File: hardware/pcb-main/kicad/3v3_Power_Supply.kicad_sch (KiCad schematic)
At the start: 15 parts, among them U1 MP2393GTL-P

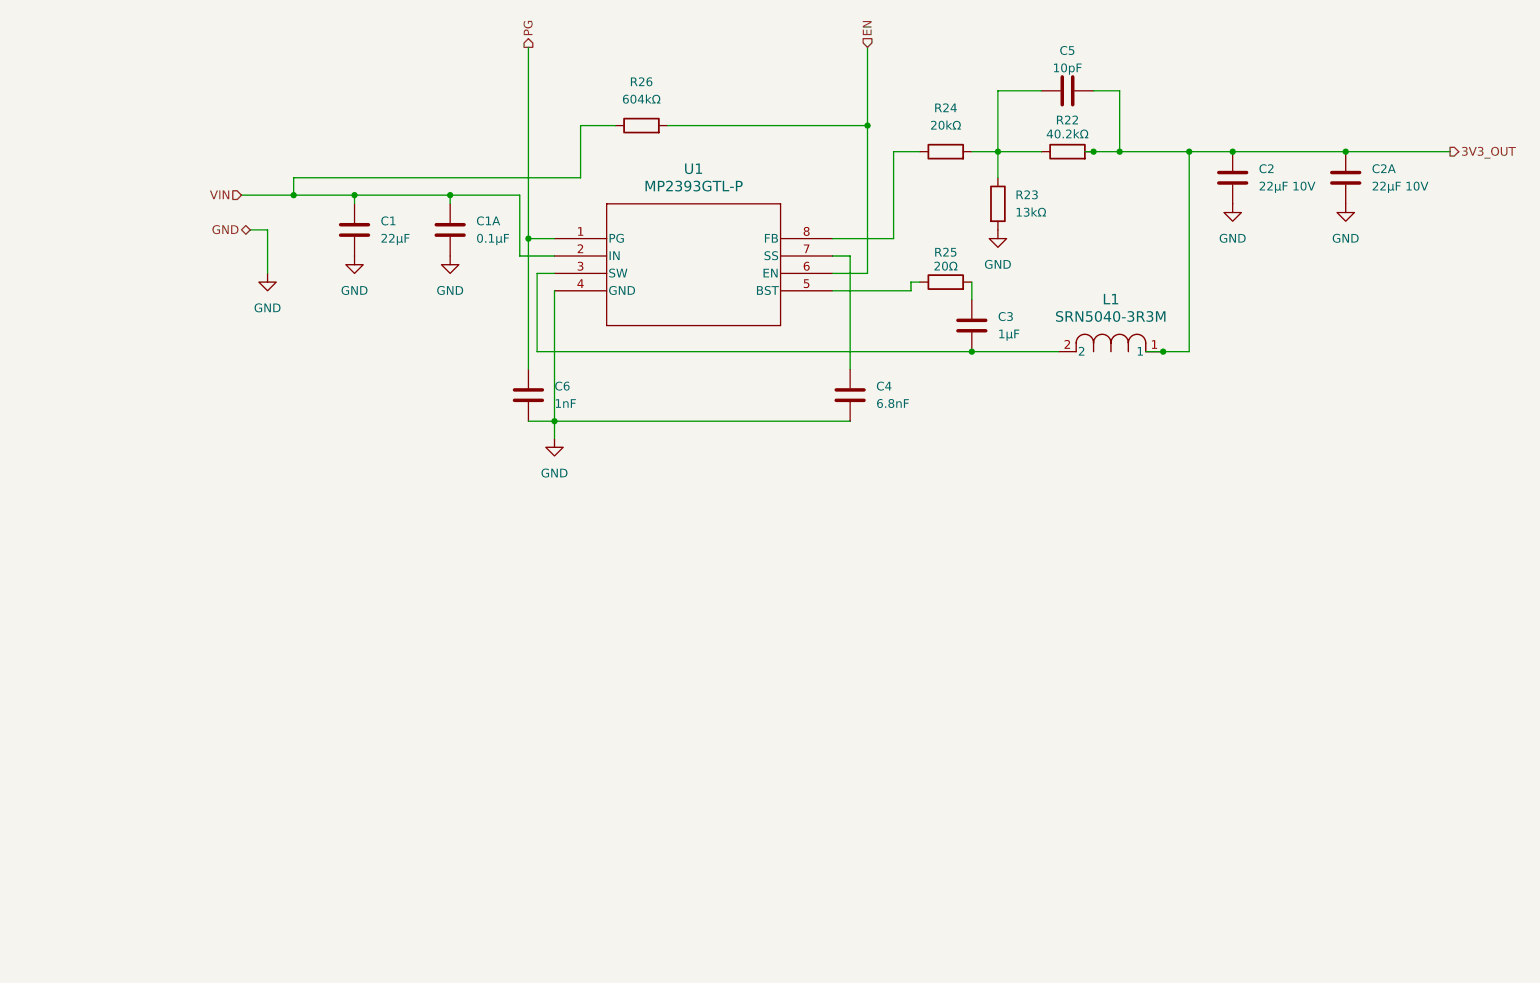
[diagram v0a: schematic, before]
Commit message: Updated to use ultra simplified 3v buck converter
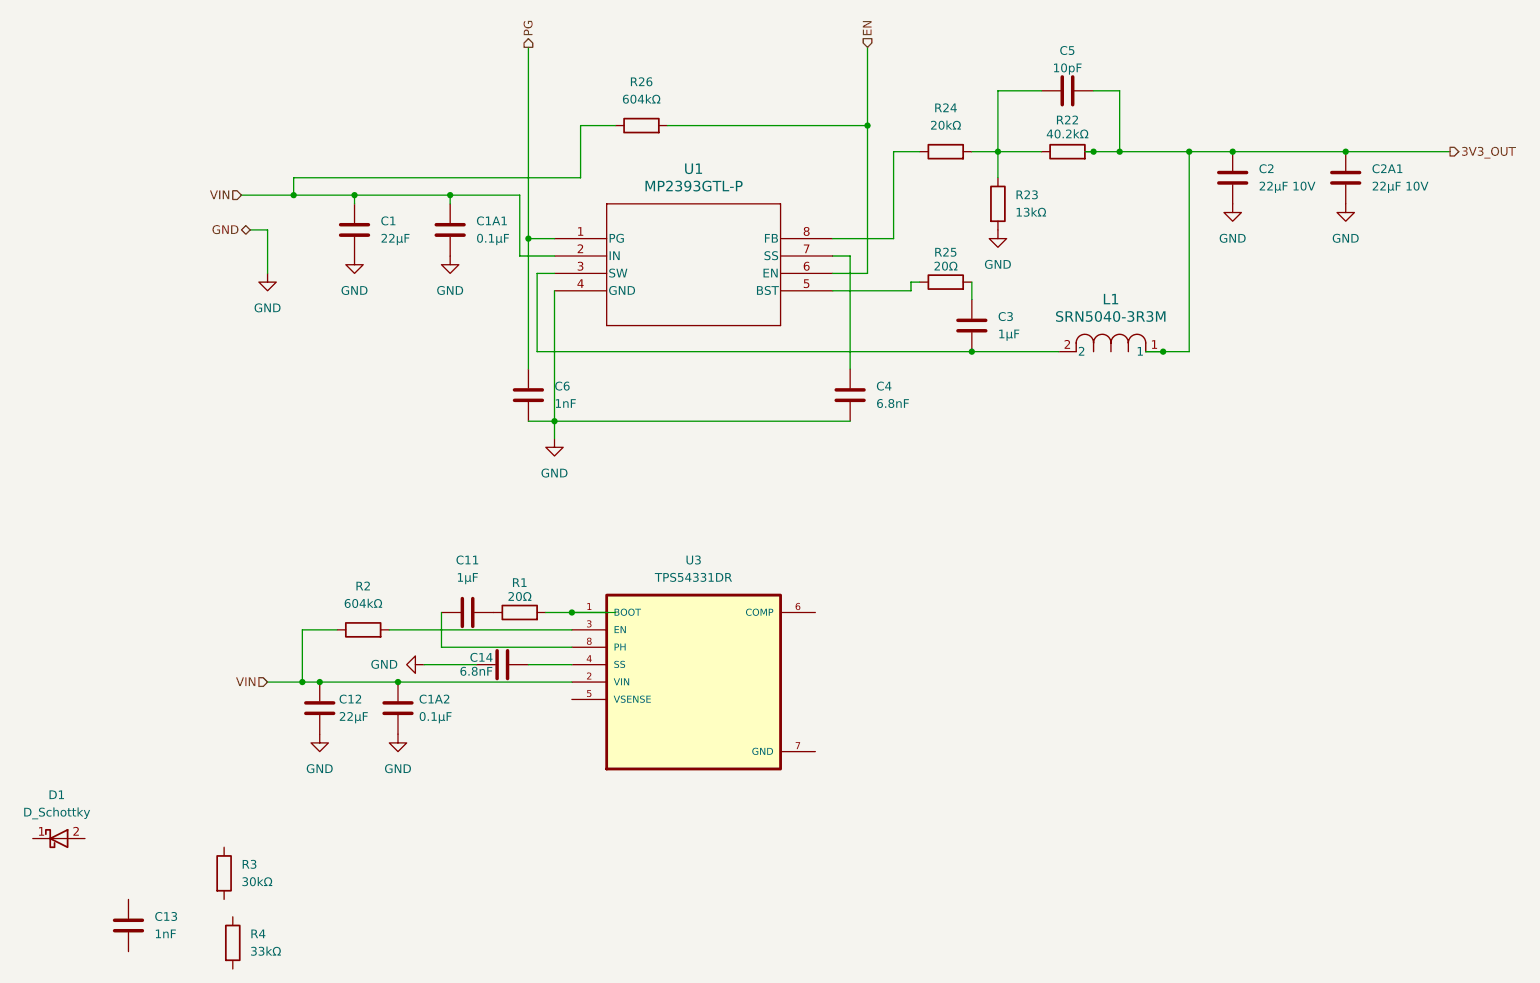
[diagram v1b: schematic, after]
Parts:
- added C11: 1µF, Capacitor_SMD:C_0603_1608Metric, symbol Device:C
- added C12: 22µF, Capacitor_SMD:C_0805_2012Metric, symbol Device:C
- added C13: 1nF, Capacitor_SMD:C_0603_1608Metric, symbol Device:C
- added C14: 6.8nF, Capacitor_SMD:C_0603_1608Metric, symbol Device:C
- added C1A2: 0.1µF, Capacitor_SMD:C_0603_1608Metric, symbol Device:C
- added D1: D_Schottky, Diode_SMD:D_SMA, symbol Device:D_Schottky
- added R1: 20Ω, Resistor_SMD:R_0603_1608Metric, symbol Device:R
- added R2: 604kΩ, Resistor_SMD:R_0603_1608Metric, symbol Device:R
- added R3: 30kΩ, Resistor_SMD:R_0603_1608Metric, symbol Device:R
- added R4: 33kΩ, Resistor_SMD:R_0603_1608Metric, symbol Device:R
- added U3: TPS54331DR, TPS54331DR:SOIC127P599X175-8N, symbol motion-play-symbols:TPS54331DR
- renumbered C1A to C1A1, C2A to C2A1
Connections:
- net GND: now also C12.2, C14.1, C1A2.2
- net VIN: now also C12.1, C1A2.1, R2.1, U3.2 (VIN)
- new net: C11.2, R1.1
- new net: R1.2, U3.1 (BOOT)
- new net: R2.2, U3.3 (EN)
- new net: C14.2, U3.4 (SS)
- new net: C11.1, U3.8 (PH)
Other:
- title: (none) -> Motion Play Main Board
